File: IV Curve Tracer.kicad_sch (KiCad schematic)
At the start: 88 parts, among them J1 9V Supply, J2 1720819, J3 CAN_In, J4 CAN_Out, Q1 IRF100P218XKMA1, Q2 IRF100P218XKMA1, SW1 SW_Push, SW2 A20303RNCG, U1 MCU_Nucleo_L432KC, U2 IES01_PDS1, U3 INA210, U4 MAX40075, U5 MAX40075, U6 ADM3055E, U7 CDSOT23-T24CAN

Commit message: theme change, ibom, pdfs, outputs generated.
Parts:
- U2: Alternative https://www.mouser.com/ProductDetail/CUI-Inc/PDS1-S5-S9-M-T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 -> (none); Alternative Part (none) -> https://www.mouser.com/ProductDetail/CUI-Inc/PDS1-S5-S9-M-T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
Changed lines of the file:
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@@
       (effects (font (size 1 1)) hide)
     )
-    (property "Alternative" "https://www.mouser.com/ProductDetail/CUI-Inc/PDS1-S5-S9-M-TR?qs=WyjlAZoYn52QMcZg5rCl5g%3D%3D" (id 11) (at 182.245 45.72 0)
+    (property "Alternative Part" "https://www.mouser.com/ProductDetail/CUI-Inc/PDS1-S5-S9-M-TR?qs=WyjlAZoYn52QMcZg5rCl5g%3D%3D" (id 11) (at 182.245 45.72 0)
       (effects (font (size 1 1)) hide)
     )

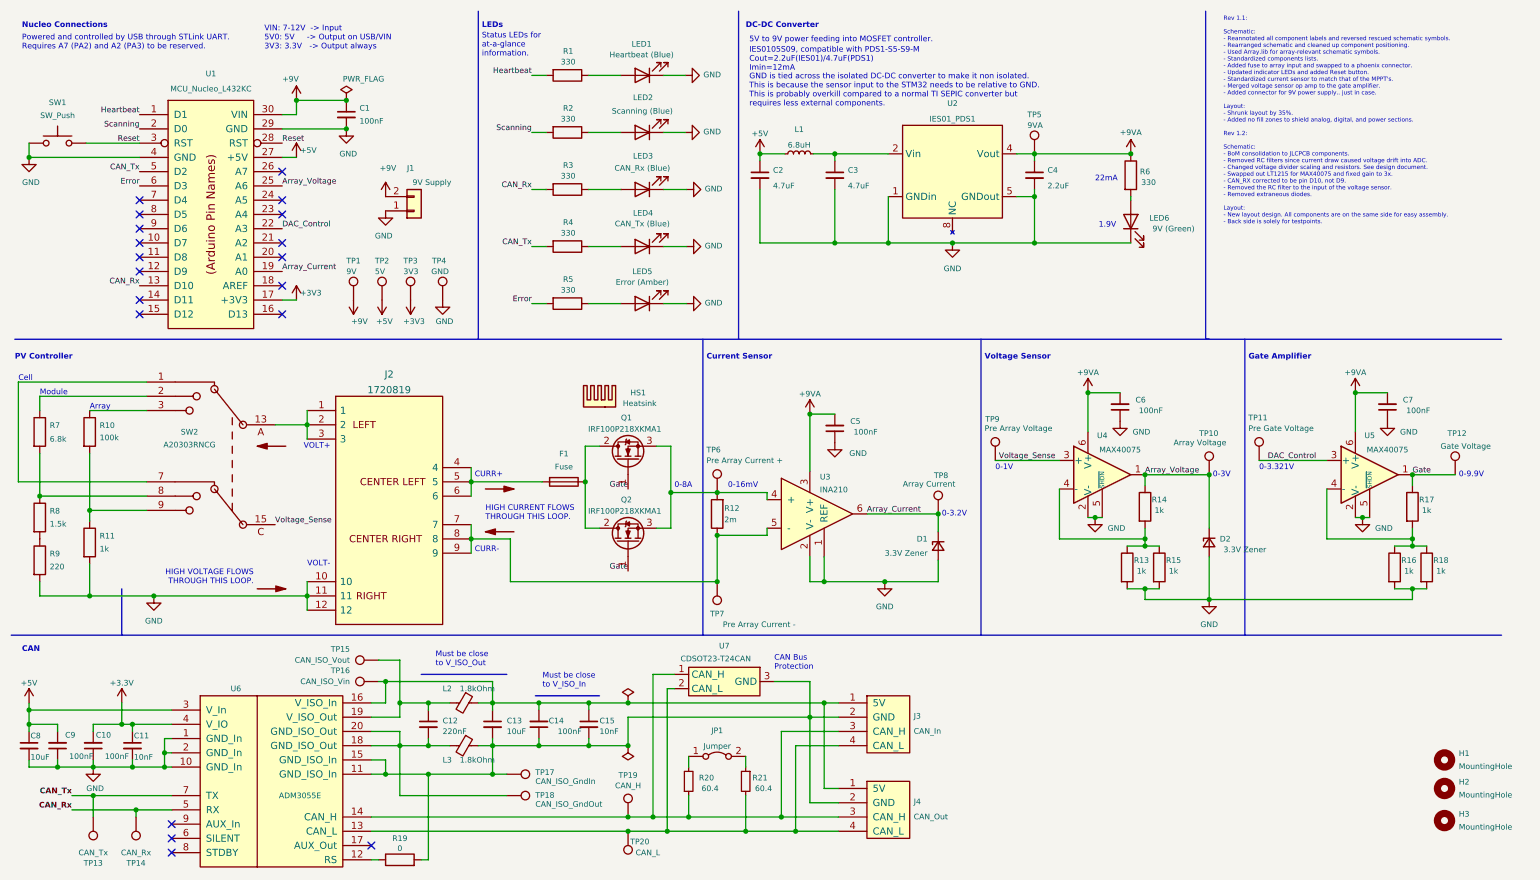
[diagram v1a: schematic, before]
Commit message: swapped INA210 to SC70 footprint, added gate resistor
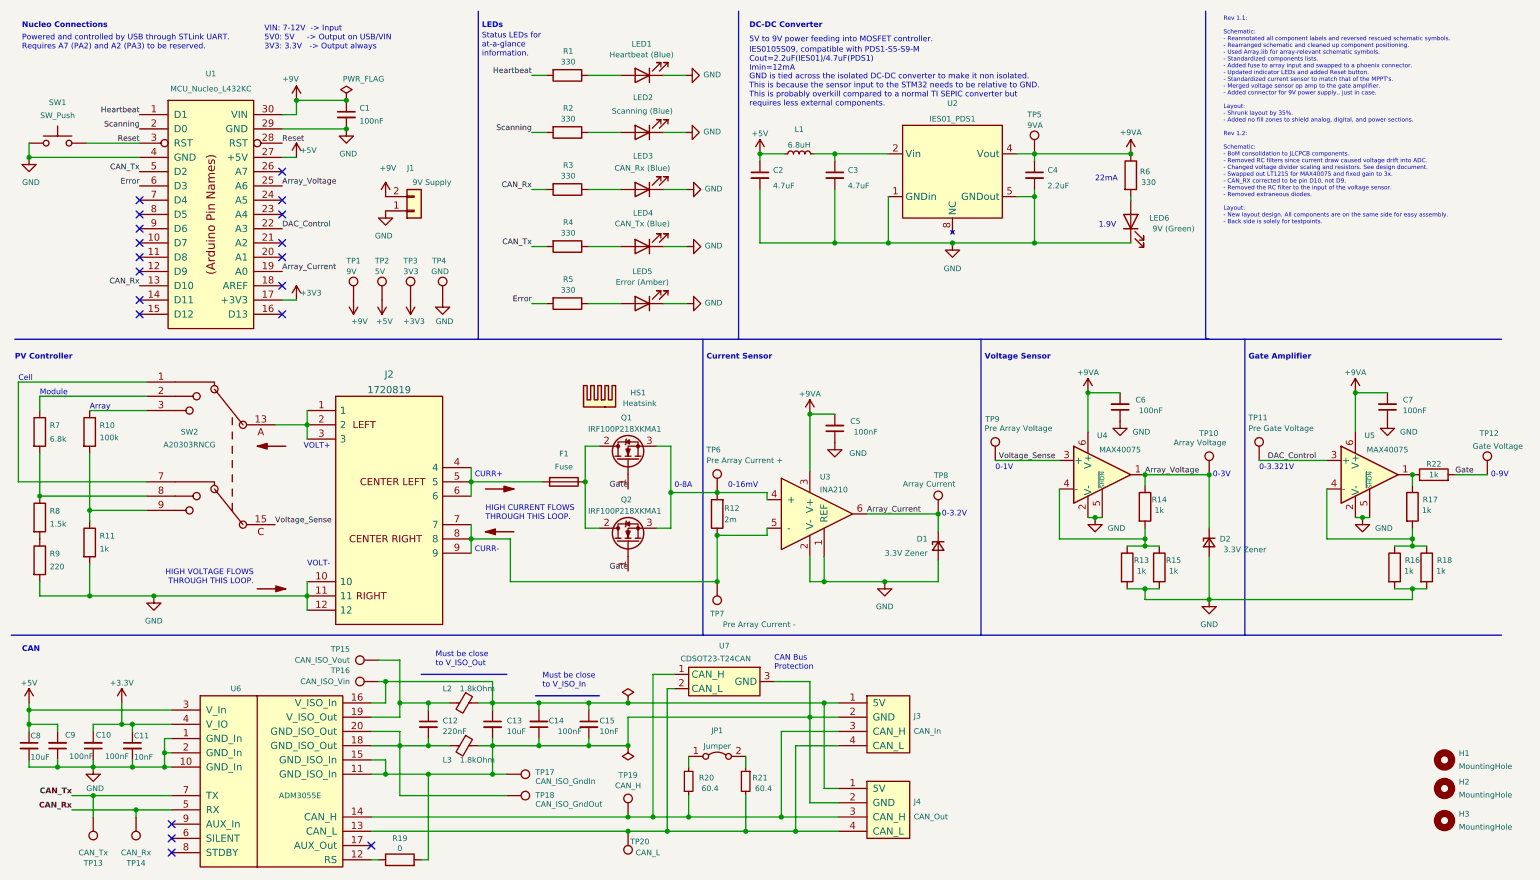
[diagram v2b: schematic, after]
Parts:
- added R22: 1k, Resistor_SMD:R_0805_2012Metric, symbol Device:R
- F1: footprint IV Curve Tracer:05200101Z_Fuze_Holder_5x20_PCB_Mount -> Footprints:05200101Z_Fuze_Holder_5x20_PCB_Mount
- J2: footprint 1720819 -> Footprints:1720819
- R12: Alternate Part https://www.mouser.com/ProductDetail/Bourns/CRF1206-FZ-R002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 -> (none); Alternative Part (none) -> https://www.mouser.com/ProductDetail/Bourns/CRF1206-FZ-R002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
- SW2: footprint IV Curve Tracer:A20303RNCG_rotary_sw_dp3t -> Footprints:A20303RNCG_rotary_sw_dp3t
- U1: footprint IV Curve Tracer:MODULE_NUCLEO-L432KC -> Footprints:MODULE_NUCLEO-L432KC
- U2: footprint IV Curve Tracer:IES01_PDS1 -> Footprints:IES01_PDS1
- U3: footprint Package_DFN_QFN:UQFN-10_1.4x1.8mm_P0.4mm -> Package_TO_SOT_SMD:SOT-363_SC-70-6_Handsoldering; Part Number INA210AIRSWT -> INA210AIDCKT; Purchase Page https://www.ti.com/store/ti/en/p/product/?p=INA210AIRSWT&HQ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 -> https://www.ti.com/store/ti/en/p/product/?p=INA210AIDCKT&HQ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
- U6: footprint IV Curve Tracer:ADM3055EBRIZ -> Footprints:ADM3055EBRIZ
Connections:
- net Gate: now also R22.2; no longer R17.1, U5.1
- new net: R17.1, R22.1, U5.1
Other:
- note added: "0-9V"
- note removed: "0-9.9V"
- moved on the sheet: TP12

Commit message: regenerated outputs and labeled output zip.
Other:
- title: Array - IV Curve Tracer -> IV Curve Tracer
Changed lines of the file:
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@@
   (paper "A4")
   (title_block
-    (title "Array - IV Curve Tracer")
-    (date "2022-02-02")
+    (title "IV Curve Tracer")
+    (date "2022-02-11")
     (rev "1.2.0")
     (company "UT Solar Vehicles Team")

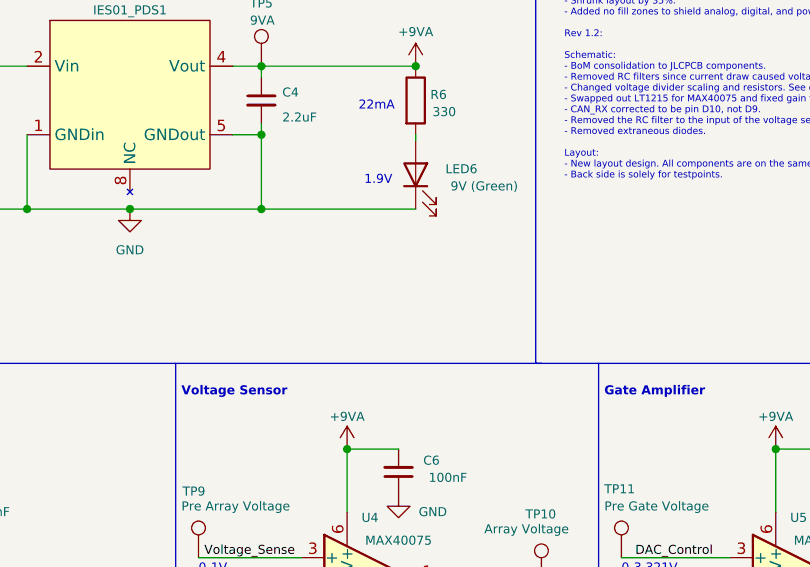
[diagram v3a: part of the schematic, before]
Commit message: gerber rebuilds to fix JLCPCB error
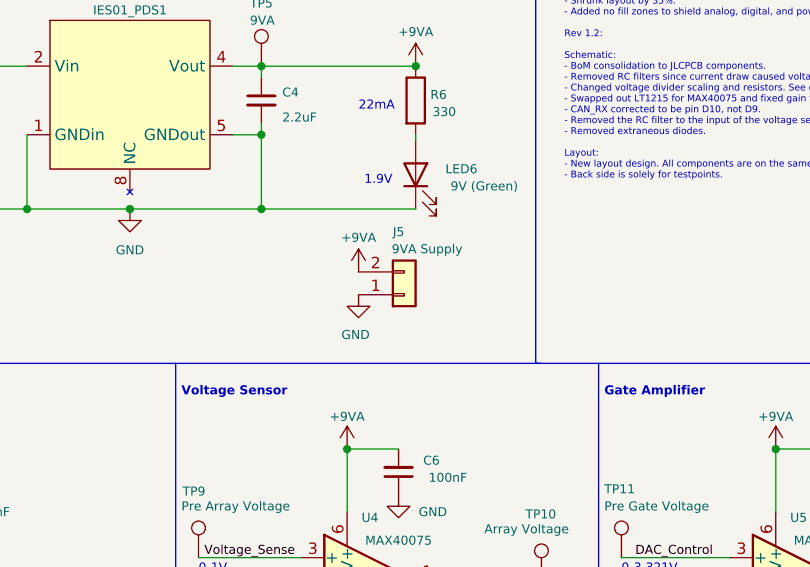
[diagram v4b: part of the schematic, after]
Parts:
- added J5: 9VA Supply, Connector_Molex:Molex_Micro-Fit_3.0_43650-0215_1x02_P3.00mm_Vertical, symbol Connector_Generic:Conn_01x02
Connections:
- net +9VA: now also J5.2 (Pin_2)
- net GND: now also J5.1 (Pin_1)
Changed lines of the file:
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@@
     )
+  )
+  (symbol (lib_id "power:+9VA") (at 207.645 66.04 0) (unit 1)
+    (in_bom yes) (on_board yes)
+    (property "Reference" "#PWR034" (id 0) (at 207.645 69.215 0)
+      (effects (font (size 1 1)) hide)
+    )
+    (property "Value" "+9VA" (id 1) (at 207.645 62.23 0)
+      (effects (font (size 1 1)))
+    )
+    (property "Footprint" "" (id 2) (at 207.645 66.04 0)
+      (effects (font (size 1 1)) hide)
+    )
+    (property "Datasheet" "" (id 3) (at 207.645 66.04 0)
+      (effects (font (size 1 1)) hide)
+    )
+    (pin "1")
   )
   (symbol (lib_id "power:GND") (at 207.645 107.95 0) (mirror y) (unit 1)
@@
     )
     (pin "1")
+  )
+  (symbol (lib_id "Connector_Generic:Conn_01x02") (at 212.725 68.58 0) (mirror x) (unit 1)
+    (in_bom yes) (on_board yes)
+    (property "Reference" "J5" (id 0) (at 212.09 61.595 0)
+      (effects (font (size 1 1)))
+    )
+    (property "Value" "9VA Supply" (id 1) (at 215.265 63.5 0)
+      (effects (font (size 1 1)))
+    )
+    (property "Footprint" "Connector_Molex:Molex_Micro-Fit_3.0_43650-0215_1x02_P3.00mm_Vertical" (id 2) (at 212.725 68.58 0)
+      (effects (font (size 1 1)) hide)
+    )
+    (property "Datasheet" "https://www.mouser.com/datasheet/2/276/0436500215_PCB_HEADERS-148687.pdf" (id 3) (at 212.725 68.58 0)
+      (effects (font (size 1 1)) hide)
+    )
+    (property "Distributor" "Mouser" (id 4) (at 212.725 68.58 0)
+      (effects (font (size 1 1)) hide)
+    )
+    (property "Manufacturer" "Molex" (id 7) (at 212.725 68.58 0)
+      (effects (font (size 1 1)) hide)
+    )
+    (property "Part Number" "538-43650-0215" (id 8) (at 212.725 68.58 0)
+      (effects (font (size 1 1)) hide)
+    )
+    (property "JLCPCB BOM" "0" (id 5) (at 212.725 68.58 0)
+      (effects (font (size 1 1)) hide)
+    )
+    (property "LCSC Part" "N/A" (id 6) (at 212.725 68.58 0)
+      (effects (font (size 1 1)) hide)
+    )
+    (property "Projected Cost" "1.46" (id 9) (at 212.725 68.58 0)
+      (effects (font (size 1 1)) hide)
+    )
+    (property "Purchase Page" "https://www.mouser.com/ProductDetail/538-43650-0215" (id 10) (at 212.725 68.58 0)
+      (effects (font (size 1 1)) hide)
+    )
+    (pin "1")
+    (pin "2")
   )
   (symbol (lib_id "Connector:TestPoint") (at 124.46 161.29 0) (unit 1)
@@
       (effects (font (size 1 1)) hide)
     )
+  )
+  (symbol (lib_id "power:GND") (at 207.645 68.58 0) (mirror y) (unit 1)
+    (in_bom yes) (on_board yes)
+    (property "Reference" "#PWR035" (id 0) (at 207.645 74.93 0)
+      (effects (font (size 1 1)) hide)
+    )
+    (property "Value" "GND" (id 1) (at 205.74 73.025 0)
+      (effects (font (size 1 1)) (justify right))
+    )
+    (property "Footprint" "" (id 2) (at 207.645 68.58 0)
+      (effects (font (size 1 1)) hide)
+    )
+    (property "Datasheet" "" (id 3) (at 207.645 68.58 0)
+      (effects (font (size 1 1)) hide)
+    )
+    (pin "1")
   )
   (symbol (lib_id "Device:FerriteBead_Small") (at 95.25 148.59 270) (unit 1)
@@
       (reference "#PWR033") (unit 1) (value "+3.3V") (footprint "")
     )
+    (path "/48fe5938-a0a4-4112-be3b-f306af368494"
+      (reference "#PWR034") (unit 1) (value "+9VA") (footprint "")
+    )
+    (path "/9bcc8639-3a93-4e97-82c0-ce38f6b90db8"
+      (reference "#PWR035") (unit 1) (value "GND") (footprint "")
+    )
     (path "/094dfbaa-522e-4327-8718-93328e6e7639"
       (reference "#SYM1") (unit 1) (value "SYM_Arrow_Normal") (footprint "")
@@
       (reference "J4") (unit 1) (value "CAN_Out") (footprint "Connector_Molex:Molex_Micro-Fit_3.0_43650-0415_1x04_P3.00mm_Vertical")
     )
+    (path "/780c110f-d675-44a5-9b77-e6d74a308504"
+      (reference "J5") (unit 1) (value "9VA Supply") (footprint "Connector_Molex:Molex_Micro-Fit_3.0_43650-0215_1x02_P3.00mm_Vertical")
+    )
     (path "/1311ed5f-6207-49d8-bef4-2159d9fdf1b6"
